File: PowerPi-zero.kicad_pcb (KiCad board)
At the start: 2 copper layers, 65 x 30 mm, 27 parts, among them J1 2444, J6 Raspberry_Pi_2_3, J8 2444, Q1 30V 4A 44mΩ, Q2 50nA 150V 200mW 200mA, Q3 30V 4A 44mΩ, U1 XL4015

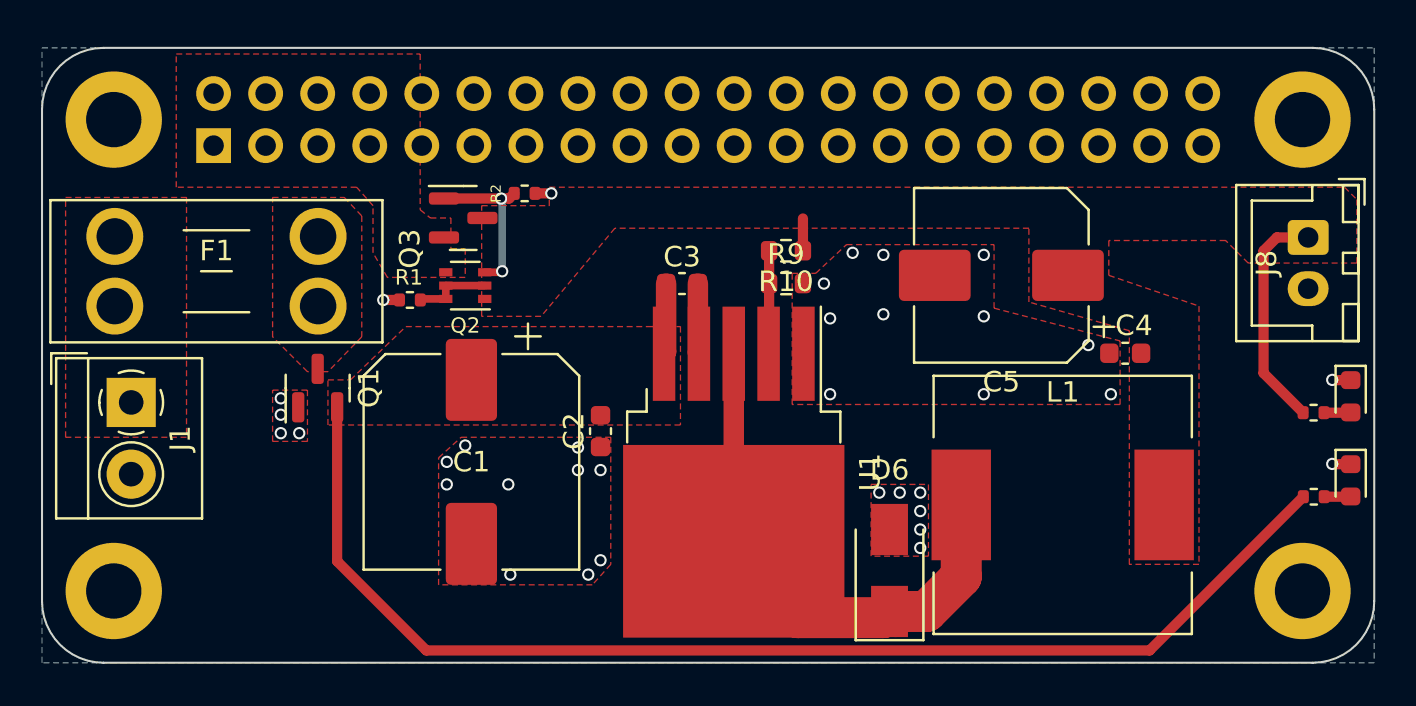
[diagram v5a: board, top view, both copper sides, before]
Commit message: Brought full design up to date with ElectriPi
Main development was done on ElectriPi so now ElectriPi mini matches those developments
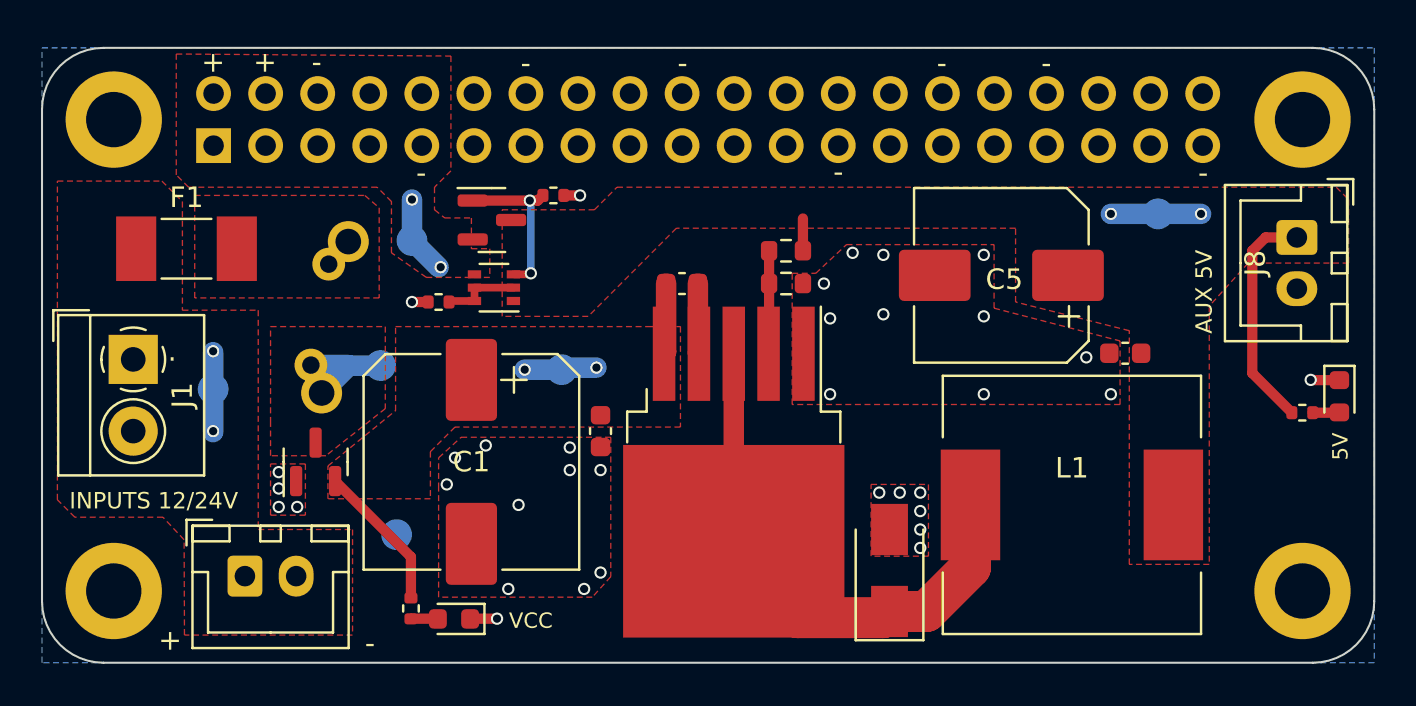
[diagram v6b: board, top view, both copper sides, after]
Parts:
- added G***: LOGO, LOGO, B.Cu at (133.2, 112.6)
- added G***: LOGO, Logos:5reen_merge_small, B.Cu at (140.6, 116.7)
- added G***: LOGO, Logos:LDO Motors Logo, B.Cu at (123.3, 117.0)
- added J2: JST XH 01x02, Connector_JST:JST_XH_B2B-XH-A_1x02_P2.50mm_Vertical, F.Cu at (99.7, 119.3)
- added TH1: ICL, Inrush_Limiter:5_OR_7pt5_PITCH_ICL, F.Cu at (104.7, 103.0)
- added TP1: TestPoint, TestPoint:TestPoint_Pad_D1.5mm, B.Cu at (144.2, 101.6)
- added TP2: TestPoint, TestPoint:TestPoint_Pad_D1.5mm, B.Cu at (98.1, 110.2)
- added TP3: TestPoint, TestPoint:TestPoint_Pad_D1.5mm, B.Cu at (106.3, 109.0)
- added TP4: TestPoint, TestPoint:TestPoint_Pad_D1.5mm, B.Cu at (115.1, 109.2)
- added TP5: TestPoint, TestPoint:TestPoint_Pad_D1.5mm, B.Cu at (107.8, 102.9)
- added TP6: TestPoint, TestPoint:TestPoint_Pad_D1.5mm, B.Cu at (107.0, 117.2)
- F1: footprint Fuse:Fuseholder_Blade_Mini_Keystone_3568 -> Fuse:Fuse_Littelfuse-NANO2-451_453
- J8: value 2444 -> JST XH 01x02
- R6: value 200 -> 1kR
- R8: value 1.5K -> 10kR
- moved R8 44.4 mm to (107.8, 120.8), turned to 90 degrees
- moved D5 44.3 mm to (109.8, 121.4), turned to 180 degrees
- moved Q1 3.60 mm to (103.1, 113.7)
- moved F1 3.55 mm to (96.8, 103.3)
- moved J1 2.10 mm to (94.2, 108.7)
- moved Q3 1.40 mm to (111.7, 101.9)
- moved R2 1.40 mm to (114.7, 100.7)
- moved Q2 1.40 mm to (111.8, 105.2)
- moved R1 1.40 mm to (109.1, 105.9)
- moved J8 0.55 mm to (151.0, 102.8)
- moved D3 0.55 mm to (153.1, 110.5)
- moved R6 0.55 mm to (151.2, 111.3)
- moved L1 0.45 mm to (140.0, 115.8)
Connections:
- Q1 pad 3: Net-(F1-Pad2) -> Net-(Q1-Pad3)
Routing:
- net VCC: track 63.0 -> 14.2 mm, vias 0 -> 2
- net Net-(Q1-Pad3): track 0.00 -> 5.27 mm
- net +5V: track 12.7 -> 17.1 mm, vias 0 -> 2
- net Net-(F1-Pad1): track 0.00 -> 3.90 mm, vias 0 -> 2
- net 5V_PI: track 0.00 -> 3.84 mm, vias 0 -> 2
- net GND: track 3.39 -> 4.30 mm
- added copper zone on F.Cu, net Net-(Q1-Pad3)
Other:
- board text added: "+"
- board text added: "-"
- board text added: "."
- board text added: "5V"
- board text added: "AUX 5V"
- board text added: "Designed by Sreenivas Eadara"
- board text added: "ElectriPi Mini by Vector 3D"
- board text added: "INPUTS 12/24V"
- board text added: "Manufactured by LDO Motors"
- board text added: "VCC"

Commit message: Updated layout, esp. component position around input side
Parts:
- moved F1 13.5 mm to (101.5, 116.0), turned to 90 degrees
- moved TH1 8.47 mm to (100.0, 110.0), turned to 90 degrees
- moved Q1 8.07 mm to (105.5, 106.0)
- moved TP6 7.95 mm to (115.0, 117.0)
- moved J2 7.55 mm to (94.0, 114.3), turned to 90 degrees
- moved TP3 7.53 mm to (103.5, 102.0)
- moved TP2 6.94 mm to (97.0, 117.0)
- moved J1 6.00 mm to (94.1, 102.7)
- moved TP5 0.92 mm to (108.0, 102.0)
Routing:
- net Net-(Q1-Pad3): track 5.27 -> 2.83 mm, vias 0 -> 2
- net VCC: track 14.2 -> 16.5 mm
- net Net-(F1-Pad1): track 3.90 -> 2.83 mm
- net 5V_PI: track 3.84 -> 3.01 mm
- net Net-(D6-Pad1): track 27.0 -> 26.4 mm
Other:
- board text added: "INPUT 12/24V"
- board text removed: "."
- board text removed: "INPUTS 12/24V"
